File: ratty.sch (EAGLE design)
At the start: 44 parts, among them IC1 L293D, Q1 BS170, Q2 BS170, Q3 BS170, Q5 BS170

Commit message: Replaced footprints to SMD for all resistors and Capacitors
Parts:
- added U$17: STM32F103_LQFP48, STM32F10x F4xx:STM32F103_LQFP48
- added U$8: FUTURA_V1.0_MOTOR_MOUNT, Futura 1.0 motor mount template:FUTURA_V1.0_MOTOR_MOUNT
- C1, C2, C3, C4, C5: device SparkFun:CAP0603-CAP -> rcl:C-EUC0603
- C12, C13, C14, C15, C6, C7, C8, C9: device SparkFun:CAP_ -> rcl:C-EUC0603
- R1, R12, R3, R4: device SparkFun:RESISTOR1206 -> rcl:R-US_R1206
- R10, R11, R13, R14, R15, R5, R6, R7: device SparkFun-Passives:RESISTORAXIAL-0.3 -> rcl:R-US_R1206
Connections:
- new net N$13: U$17.VSS_3
- new net N$14: U$17.PA4
- new net N$17: U$17.PB0
- new net N$18: U$17.PB7
- new net N$19: U$17.VDD_2
- new net N$2: U$17.VDD_3
- new net N$20: U$17.VSS_2
- new net N$21: U$17.VSSA
- new net N$22: U$17.VDDA
- new net PA_0_ENCODER1: U$17.PA0-WKUP
- new net PA_1_ENCODER1: U$17.PA1
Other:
- moved on the sheet: C1, C12, C13, C14, C15, C4, C5, C6, C7, C8, C9

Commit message: Added gyro and some paths for MCU
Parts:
- removed U$17: STM32F103_LQFP48, STM32F10x F4xx:STM32F103_LQFP48
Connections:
- removed net N$13: U$17.VSS_3
- removed net N$14: U$17.PA4
- removed net N$17: U$17.PB0
- removed net N$18: U$17.PB7
- removed net N$19: U$17.VDD_2
- removed net N$2: U$17.VDD_3
- removed net N$20: U$17.VSS_2
- removed net N$21: U$17.VSSA
- removed net N$22: U$17.VDDA
- removed net PA_0: R1.2, U$4.PA0, U$6.E
- removed net PA_0_ENCODER1: U$17.PA0-WKUP
- removed net PA_1_ENCODER1: U$17.PA1
- removed net PA_4: R3.2, U$4.PA4, U$9.E
- new net PA_0_ENCODER1_1: U$4.PA0
- new net PA_1_ENCODER1_2: U$4.PA1
- new net PA_2_ENCODER2_1: U$4.PA2
- new net PA_3_ENCODER2_2: U$4.PA3
- new net PA_5: R1.2, U$4.PA5, U$6.E
- new net PA_6: R3.2, U$4.PA6, U$9.E

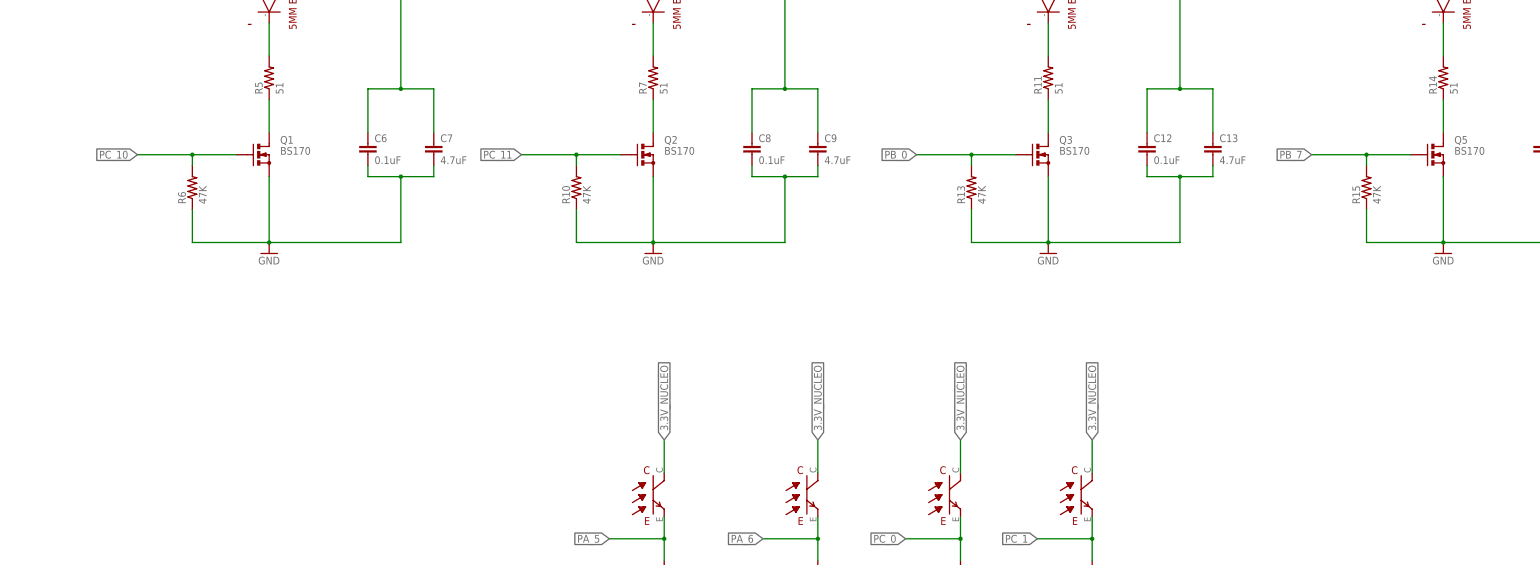
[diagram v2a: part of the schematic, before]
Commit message: Resistor values updated
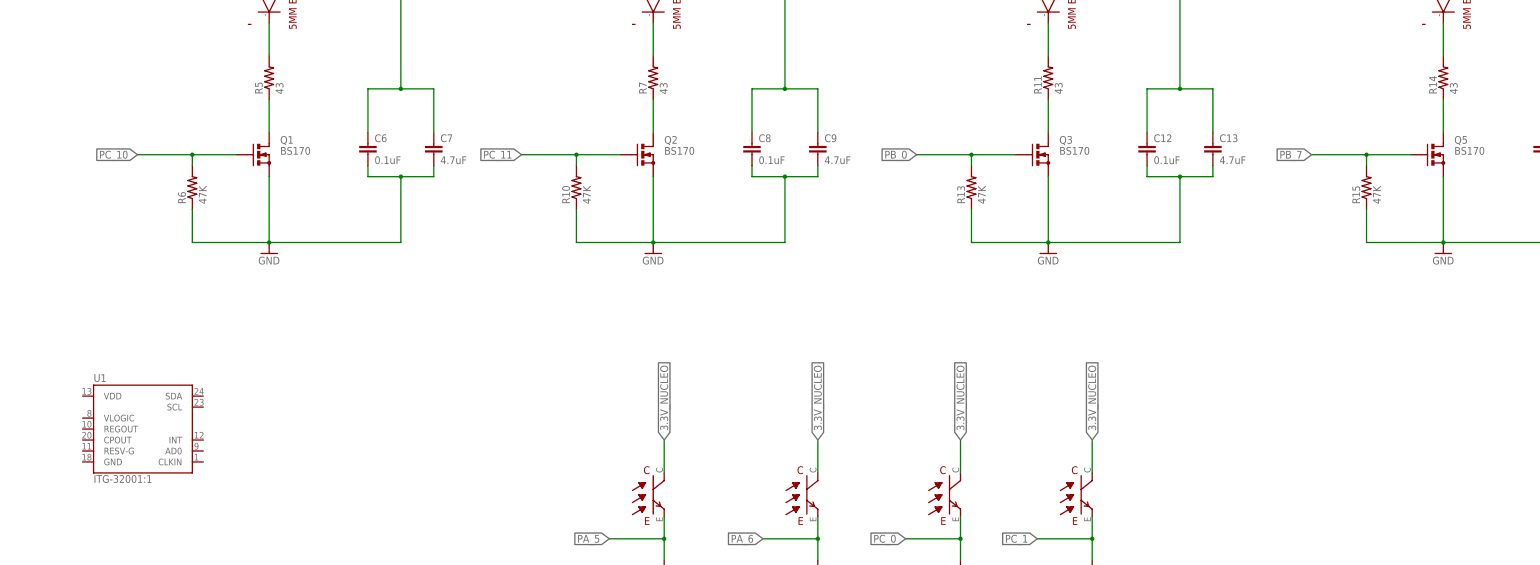
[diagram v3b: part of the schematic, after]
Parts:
- added U1: ITG-32001:1, SparkFun-Sensors:ITG-32001:1
- R11, R14, R5, R7: value 51 -> 43
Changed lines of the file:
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@@
 <part name="U$12" library="SparkFun-Aesthetics" deviceset="AGND" device=""/>
 <part name="U$15" library="sfh4550 &amp; teft4300" deviceset="EMITTER" device=""/>
-<part name="R5" library="rcl" deviceset="R-US_" device="R1206" value="51"/>
+<part name="R5" library="rcl" deviceset="R-US_" device="R1206" value="43"/>
 <part name="R6" library="rcl" deviceset="R-US_" device="R1206" value="47K"/>
 <part name="Q1" library="transistor-small-signal" deviceset="BS170" device=""/>
@@
 <part name="C7" library="rcl" deviceset="C-EU" device="C0603" value="4.7uF"/>
 <part name="U$16" library="sfh4550 &amp; teft4300" deviceset="EMITTER" device=""/>
-<part name="R7" library="rcl" deviceset="R-US_" device="R1206" value="51"/>
+<part name="R7" library="rcl" deviceset="R-US_" device="R1206" value="43"/>
 <part name="R10" library="rcl" deviceset="R-US_" device="R1206" value="47K"/>
 <part name="Q2" library="transistor-small-signal" deviceset="BS170" device=""/>
@@
 <part name="C9" library="rcl" deviceset="C-EU" device="C0603" value="4.7uF"/>
 <part name="U$18" library="sfh4550 &amp; teft4300" deviceset="EMITTER" device=""/>
-<part name="R11" library="rcl" deviceset="R-US_" device="R1206" value="51"/>
+<part name="R11" library="rcl" deviceset="R-US_" device="R1206" value="43"/>
 <part name="R13" library="rcl" deviceset="R-US_" device="R1206" value="47K"/>
 <part name="Q3" library="transistor-small-signal" deviceset="BS170" device=""/>
@@
 <part name="C13" library="rcl" deviceset="C-EU" device="C0603" value="4.7uF"/>
 <part name="U$19" library="sfh4550 &amp; teft4300" deviceset="EMITTER" device=""/>
-<part name="R14" library="rcl" deviceset="R-US_" device="R1206" value="51"/>
+<part name="R14" library="rcl" deviceset="R-US_" device="R1206" value="43"/>
 <part name="R15" library="rcl" deviceset="R-US_" device="R1206" value="47K"/>
 <part name="Q5" library="transistor-small-signal" deviceset="BS170" device=""/>
@@
 <part name="U$4" library="stm32f411" deviceset="STM32F411XC" device=""/>
 <part name="U$8" library="Futura 1.0 motor mount template" deviceset="FUTURA_V1.0_MOTOR_MOUNT" device=""/>
+<part name="U1" library="SparkFun-Sensors" deviceset="ITG-3200" device="1:1"/>
 </parts>
 <sheets>
@@
 <instance part="U$4" gate="G$1" x="147.32" y="251.46"/>
 <instance part="U$8" gate="G$1" x="363.22" y="7.62"/>
+<instance part="U1" gate="G$1" x="231.14" y="152.4"/>
 </instances>
 <busses>

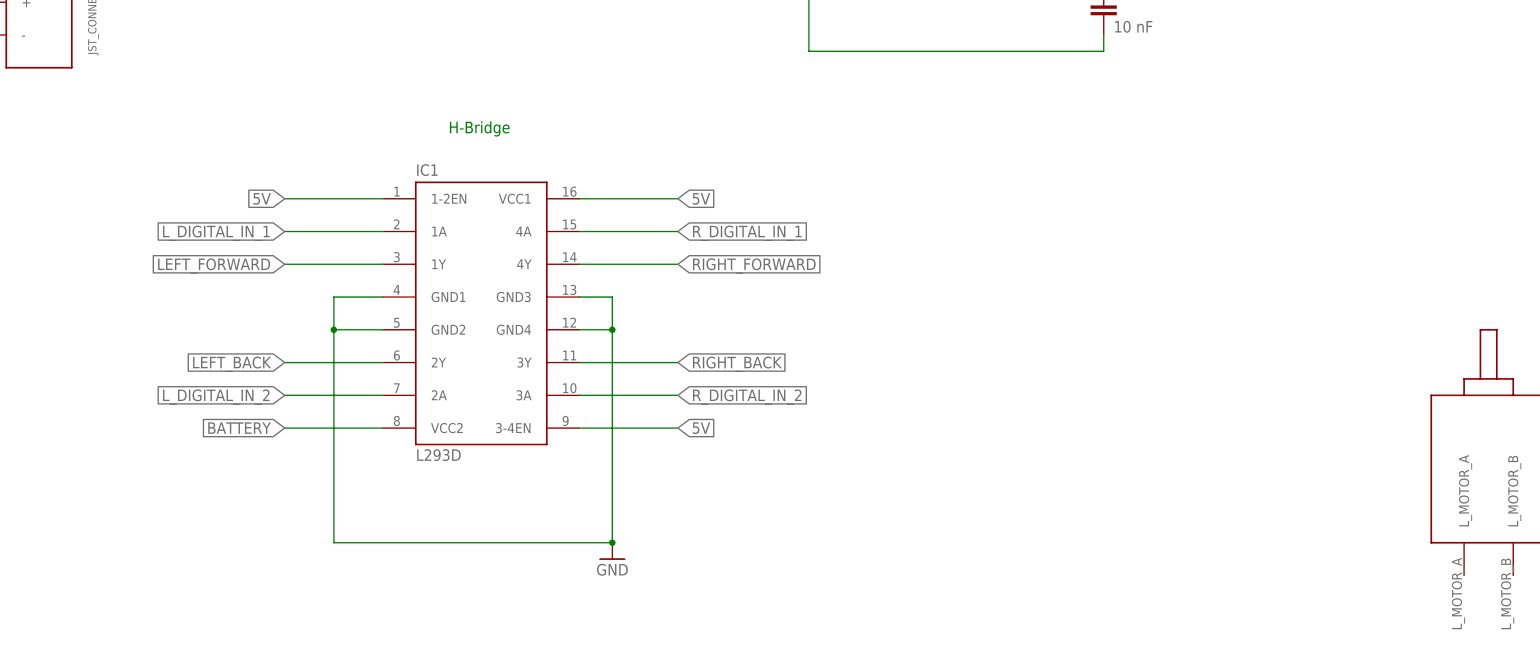
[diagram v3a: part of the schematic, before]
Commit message: Switched L239D to L239DD
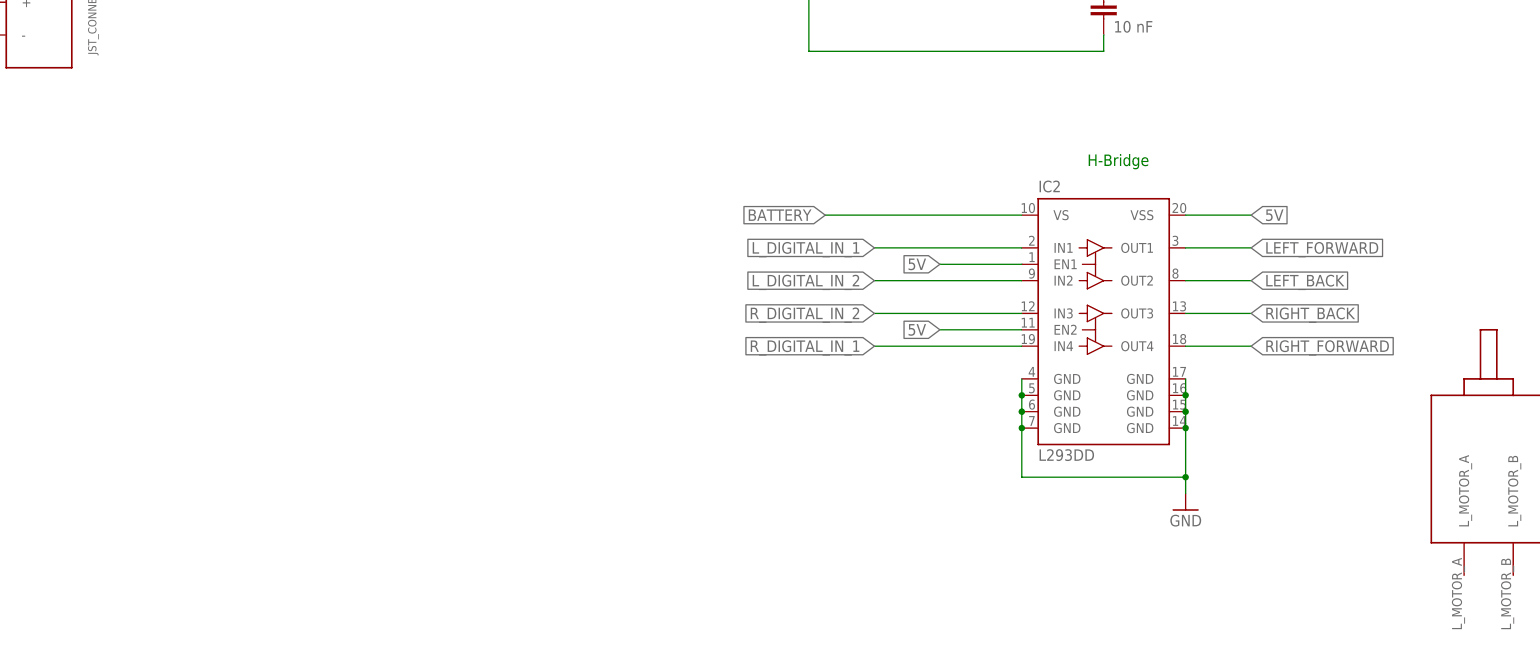
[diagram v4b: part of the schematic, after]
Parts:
- removed IC1: L293D, st-microelectronics:L293D
- added IC2: L293DD, st-microelectronics:L293DD
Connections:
- net 5V: now also IC2.EN1, IC2.EN2, IC2.VSS; no longer IC1.1-2EN, IC1.3-4EN, IC1.VCC1
- net BATTERY: now also IC2.VS; no longer IC1.VCC2
- net GND: now also IC2.GND@1, IC2.GND@2, IC2.GND@3, IC2.GND@4, IC2.GND@5, IC2.GND@6, IC2.GND@7, IC2.GND@8; no longer IC1.GND1, IC1.GND2, IC1.GND3, IC1.GND4
- net LEFT_BACK: now also IC2.OUT2; no longer IC1.2Y
- net LEFT_FORWARD: now also IC2.OUT1; no longer IC1.1Y
- net L_DIGITAL_IN_1: now also IC2.IN1; no longer IC1.1A
- net L_DIGITAL_IN_2: now also IC2.IN2; no longer IC1.2A
- net RIGHT_BACK: now also IC2.OUT3; no longer IC1.3Y
- net RIGHT_FORWARD: now also IC2.OUT4; no longer IC1.4Y
- net R_DIGITAL_IN_1: now also IC2.IN4; no longer IC1.4A
- net R_DIGITAL_IN_2: now also IC2.IN3; no longer IC1.3A

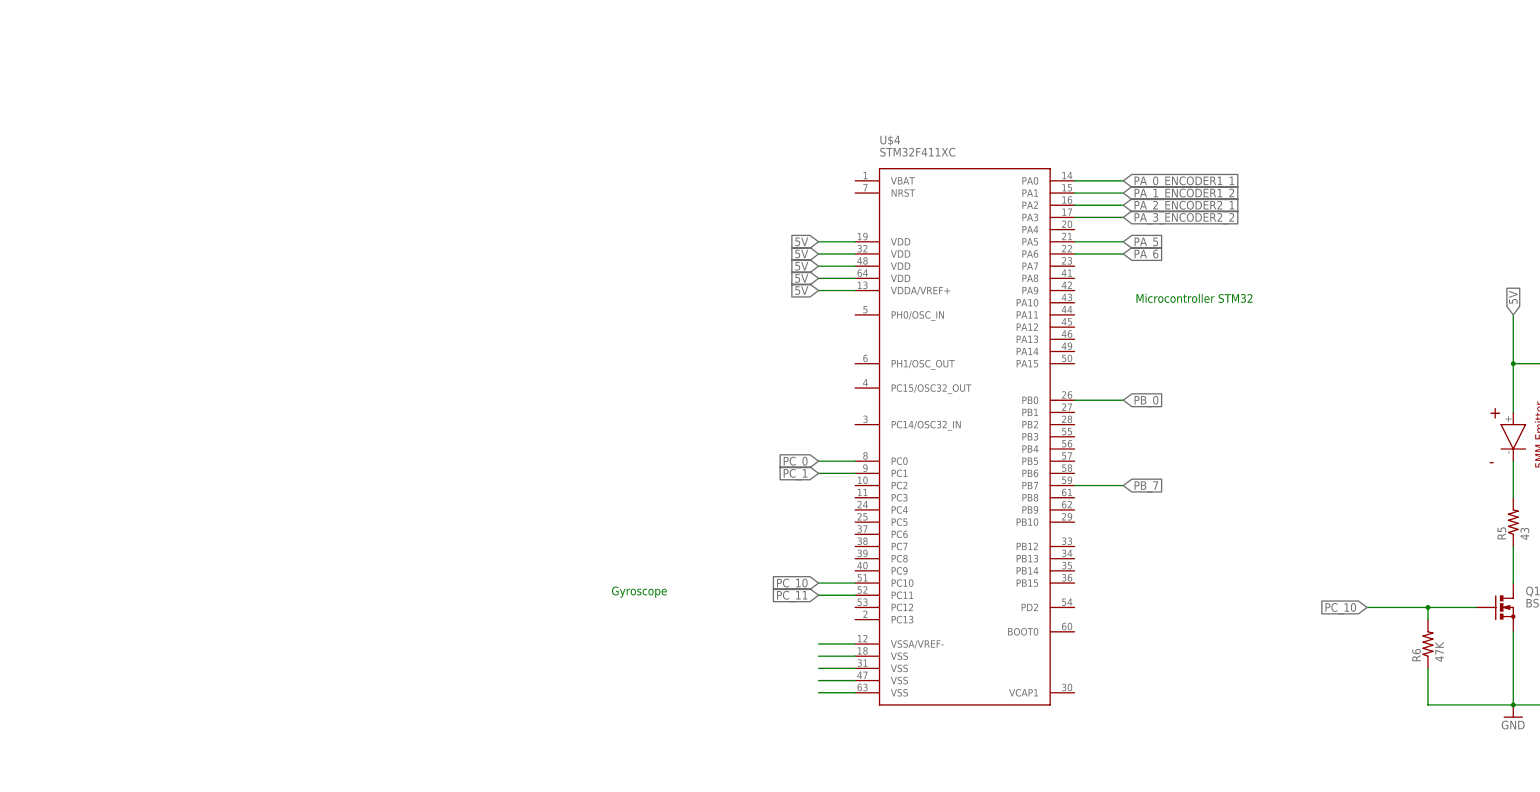
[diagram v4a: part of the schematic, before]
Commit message: Added MCU related things
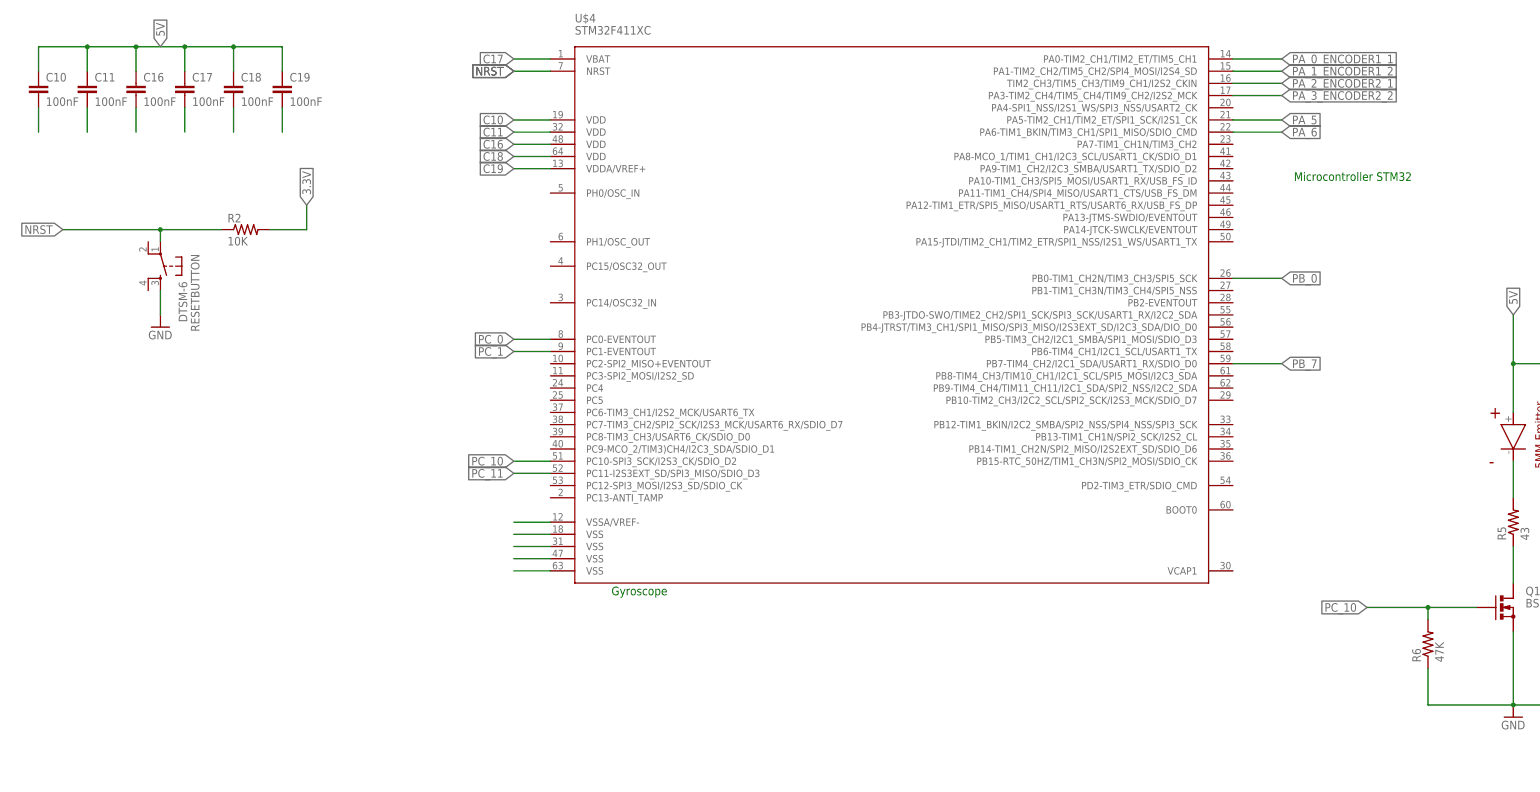
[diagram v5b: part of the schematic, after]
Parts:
- added C10, C11, C16, C17, C18, C19: 100nF, rcl:C-EUC0603
- added R2: 10K, rcl:R-US_R1206
- added RESETBUTTON: DTSM-6, switch-tact:DTSM-6
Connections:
- removed net PA_0_ENCODER1_1: U$4.PA0
- removed net PA_1_ENCODER1_2: U$4.PA1
- removed net PA_2_ENCODER2_1: U$4.PA2
- removed net PA_3_ENCODER2_2: U$4.PA3
- new net C10: C10.2
- new net C11: C11.2
- new net C16: C16.2
- new net C17: C17.2, U$4.VBAT
- new net C18: C18.2
- new net C19: C19.2
- new net NRST: R2.1, RESETBUTTON.1, U$4.NRST
- net 3.3V: now also R2.2
- net 5V: now also C10.1, C11.1, C16.1, C17.1, C18.1, C19.1; no longer U$4.VDD@1, U$4.VDD@2, U$4.VDD@3, U$4.VDD@4, U$4.VDDA/VREF+
- net GND: now also RESETBUTTON.3; no longer U$4.VSS@1, U$4.VSS@2, U$4.VSS@3, U$4.VSS@4, U$4.VSSA/VREF-
- net PA_5: no longer U$4.PA5
- net PA_6: no longer U$4.PA6
- net PB_0: no longer U$4.PB0
- net PB_7: no longer U$4.PB7
- net PC_0: no longer U$4.PC0
- net PC_1: no longer U$4.PC1
- net PC_10: no longer U$4.PC10
- net PC_11: no longer U$4.PC11
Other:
- moved on the sheet: U$4

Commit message: Added gyro
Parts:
- added C20: 10nF, rcl:C-EUC0603
- added C21, C22: 0.1uF, rcl:C-EUC0603
- added C23: 2.2nF, rcl:C-EUC0603
- added U$17: SPLITTER, splitter:SPLITTER
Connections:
- new net GRYOREGOUT: U1.REGOUT
- new net GRYOVLOGIC: U1.VLOGIC
- new net GYROCPOUT: C23.1, U1.CPOUT
- new net GYROREGOUT: C21.1
- new net GYROVDD: C22.1, U1.VDD
- new net GYROVLOGIC: C20.1
- net GND: now also C20.2, C21.2, C22.2, C23.2, U1.GND, U1.RESV-G
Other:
- moved on the sheet: R1, R12, R3, R4
